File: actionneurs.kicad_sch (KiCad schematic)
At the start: 73 parts, among them J1 690367280876, J10 ESC_35_1_P, J11 690367280876, J12 ESC_35_2_S, J13 Alim Pompe, J14 690367280876, J6 ESC_35_1_P, J7 RGBA_LEDs, J9 ESC_35_1_S, Q1 G2302, Q10 G2302, Q11 G2302, Q12 G2302, Q13 G2302, Q14 G2302, Q15 G2302, Q16 G2302, Q17 G2302, Q2 G2302, Q3 G2302, Q4 G2302, Q5 G2302, Q9 G2302

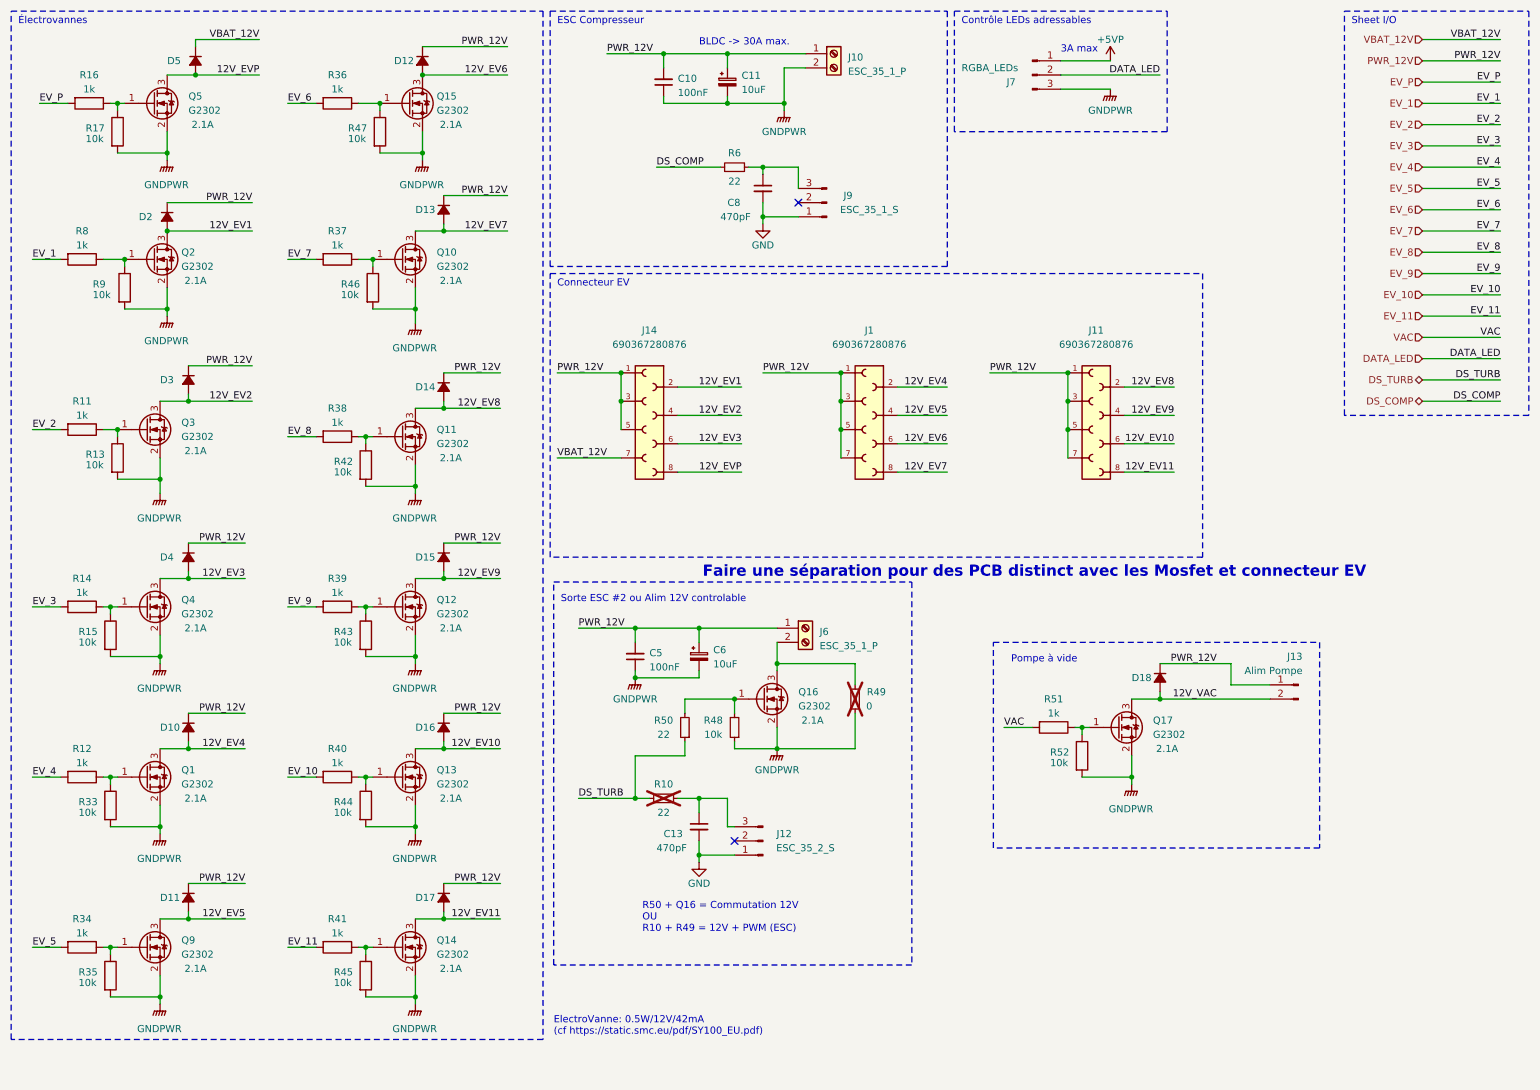
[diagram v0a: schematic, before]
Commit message: split des cartes
Todo: sync routage et ajout trou de fixation
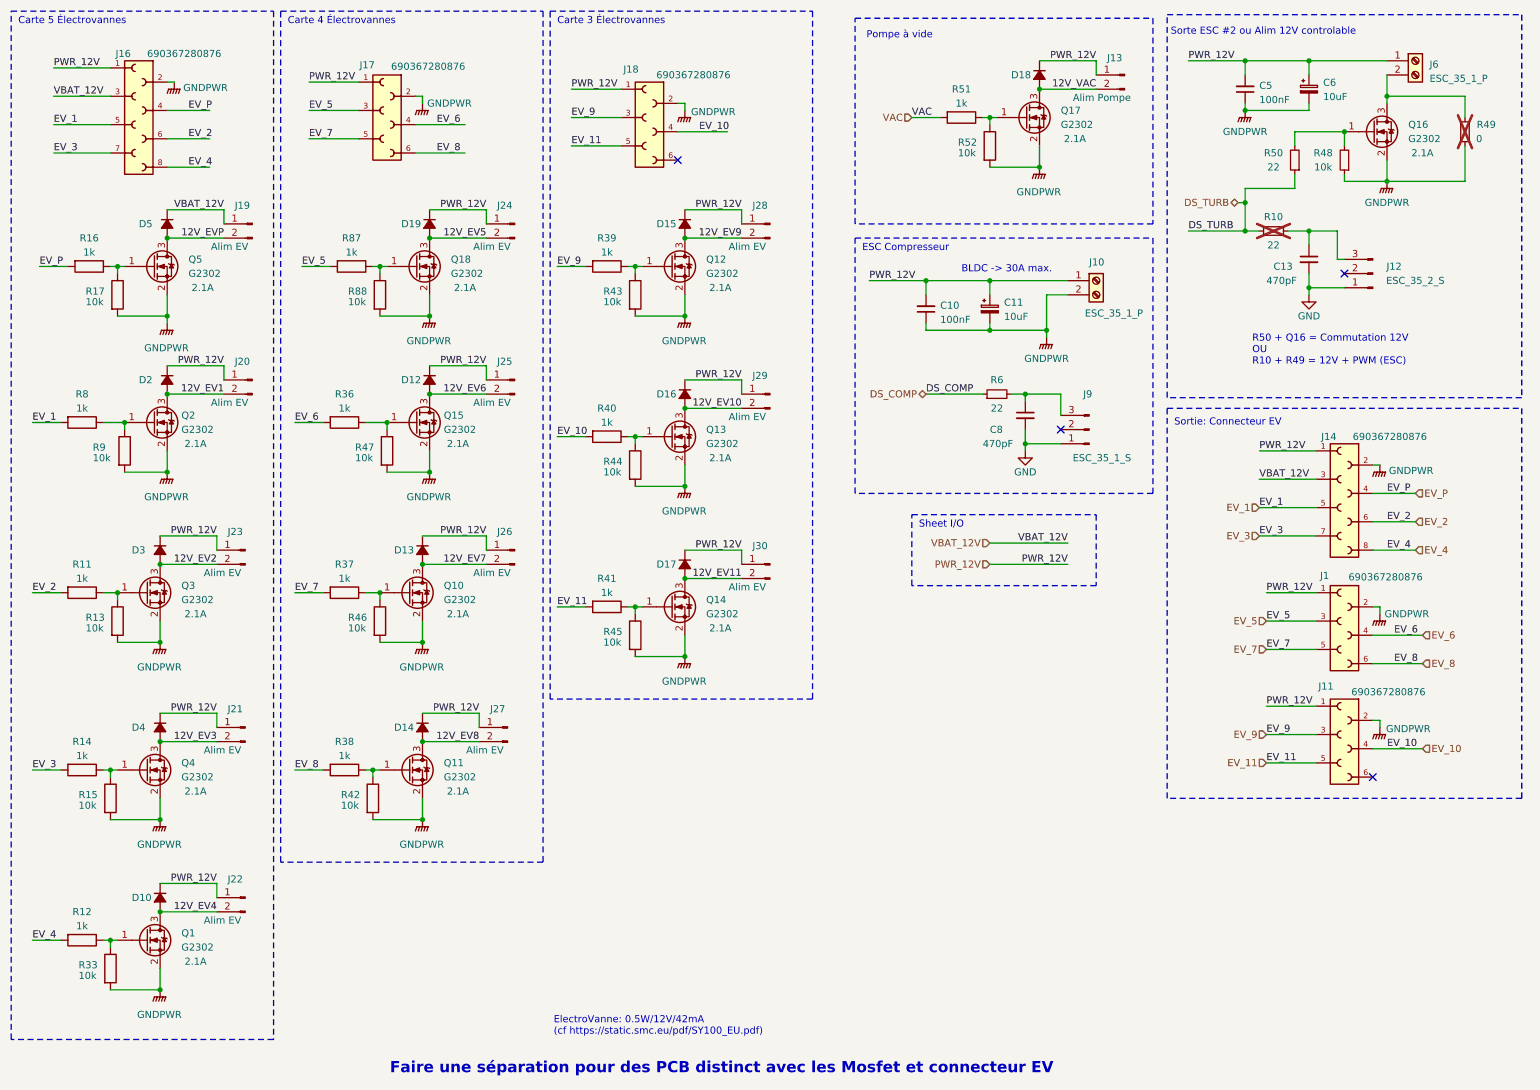
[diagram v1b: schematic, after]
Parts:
- removed D11: ~, Diode_SMD:D_SOD-123F, symbol Device:D_Small_Filled
- removed J7: RGBA_LEDs, Connector_PinHeader_2.54mm:PinHeader_1x03_P2.54mm_Vertical, symbol Connector:Conn_01x03_Pin
- removed Q9: G2302, Package_TO_SOT_SMD:SOT-23, symbol Device:Q_NMOS_GSD
- removed R34: 1k, Resistor_SMD:R_0603_1608Metric, symbol Device:R
- removed R35: 10k, Resistor_SMD:R_0603_1608Metric, symbol Device:R
- added D19: ~, Diode_SMD:D_SOD-123F, symbol Device:D_Small_Filled
- added J16: 690367280876, ConnectorsEvo:690367280876, symbol ConnectorsEvo:690367280876
- added J17, J18: 690367280876, ConnectorsEvo:690367280676, symbol ConnectorsEvo:690367280676
- added J19, J20, J21, J22, J23, J24, J25, J26, J27, J28, J29, J30: Alim EV, Connector_PinSocket_2.54mm:PinSocket_1x02_P2.54mm_Vertical, symbol Connector:Conn_01x02_Pin
- added Q18: G2302, Package_TO_SOT_SMD:SOT-23, symbol Device:Q_NMOS_GSD
- added R87: 1k, Resistor_SMD:R_0603_1608Metric, symbol Device:R
- added R88: 10k, Resistor_SMD:R_0603_1608Metric, symbol Device:R
- J1, J11: footprint ConnectorsEvo:690367280876 -> ConnectorsEvo:690367280676; symbol ConnectorsEvo:690367280876 -> ConnectorsEvo:690367280676; PART-NUMBER 690367280876 -> 690367280676; PINS 8 -> 6
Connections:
- net 12V_EV1: now also J20.2 (Pin_2); no longer J14.2
- net 12V_EV10: now also J29.2 (Pin_2); no longer J11.6
- net 12V_EV11: now also J30.2 (Pin_2); no longer J11.8
- net 12V_EV2: now also J23.2 (Pin_2); no longer J14.4
- net 12V_EV3: now also J21.2 (Pin_2); no longer J14.6
- net 12V_EV4: now also J22.2 (Pin_2); no longer J1.2
- net 12V_EV5: now also D19.2 (A), J24.2 (Pin_2), Q18.3 (D); no longer J1.4
- net 12V_EV6: now also J25.2 (Pin_2); no longer J1.6
- net 12V_EV7: now also J26.2 (Pin_2); no longer J1.8
- net 12V_EV8: now also J27.2 (Pin_2); no longer J11.2
- net 12V_EV9: now also J28.2 (Pin_2); no longer J11.4
- net 12V_EVP: now also J19.2 (Pin_2); no longer J14.8
- net EV_1: now also J14.5, J16.5
- net EV_10: now also J11.4, J18.4
- net EV_11: now also J11.5, J18.5
- net EV_2: now also J14.6, J16.6
- net EV_3: now also J14.7, J16.7
- net EV_4: now also J14.8, J16.8
- net EV_5: now also J1.3, J17.3, R87.2
- net EV_6: now also J1.4, J17.4
- net EV_7: now also J1.5, J17.5
- net EV_8: now also J1.6, J17.6
- net EV_9: now also J11.3, J18.3
- net EV_P: now also J14.4, J16.4
- net GNDPWR: now also J1.2, J11.2, J14.2, J16.2, J17.2, J18.2, Q18.2 (S), R88.2
- net PWR_12V: now also D19.1 (K), J16.1, J17.1, J18.1, J20.1 (Pin_1), J21.1 (Pin_1), J22.1 (Pin_1), J23.1 (Pin_1), J24.1 (Pin_1), J25.1 (Pin_1), J26.1 (Pin_1), J27.1 (Pin_1), J28.1 (Pin_1), J29.1 (Pin_1), J30.1 (Pin_1); no longer J1.3, J1.5, J1.7, J11.3, J11.5, J11.7, J14.3, J14.5
- net VBAT_12V: now also J14.3, J16.3, J19.1 (Pin_1); no longer J14.7
- new net: Q18.1 (G), R87.1, R88.1
- no-connect marks 2 -> 4
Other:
- note added: "Carte 3 Électrovannes"
- note added: "Carte 4 Électrovannes"
- note added: "Carte 5 Électrovannes"
- note added: "Sortie: Connecteur EV"
- note removed: "3A max"
- note removed: "Connecteur EV"
- note removed: "Contrôle LEDs adressables"
- note removed: "Électrovannes"
- moved on the sheet: C10, C11, C13, C5, C6, C8, D10, D12, D13, D14, D18, D2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

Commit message: optimisation empreinte passif (TODO fp diode), TODO ajouter LED temoin diverse, groupement sur PCB des nouveaux composant
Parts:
- R49: footprint Resistor_SMD:R_0603_1608Metric -> Jumper:SolderJumper-2_P1.3mm_Open_RoundedPad1.0x1.5mm; symbol Device:R_Small -> Jumper:SolderJumper_2_Open
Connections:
- net EV_1: now also J14.3, J16.3; no longer J14.5, J16.5
- net EV_2: now also J14.4, J16.4; no longer J14.6, J16.6
- net EV_3: now also J14.5, J16.5; no longer J14.7, J16.7
- net EV_4: now also J14.6, J16.6; no longer J14.8, J16.8
- net EV_P: now also J14.8, J16.8; no longer J14.4, J16.4
- net GNDPWR: now also R49.2 (B); no longer R49.1
- net VBAT_12V: now also J14.7, J16.7; no longer J14.3, J16.3
- net at J6.2 (Pin_2), Q16.3 (D): now also R49.1 (A); no longer R49.2
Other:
- note removed: "Faire une séparation pour des PCB distinct avec les Mosfet et connecteur EV"
- moved on the sheet: C5, C6, Q16, R48, R50

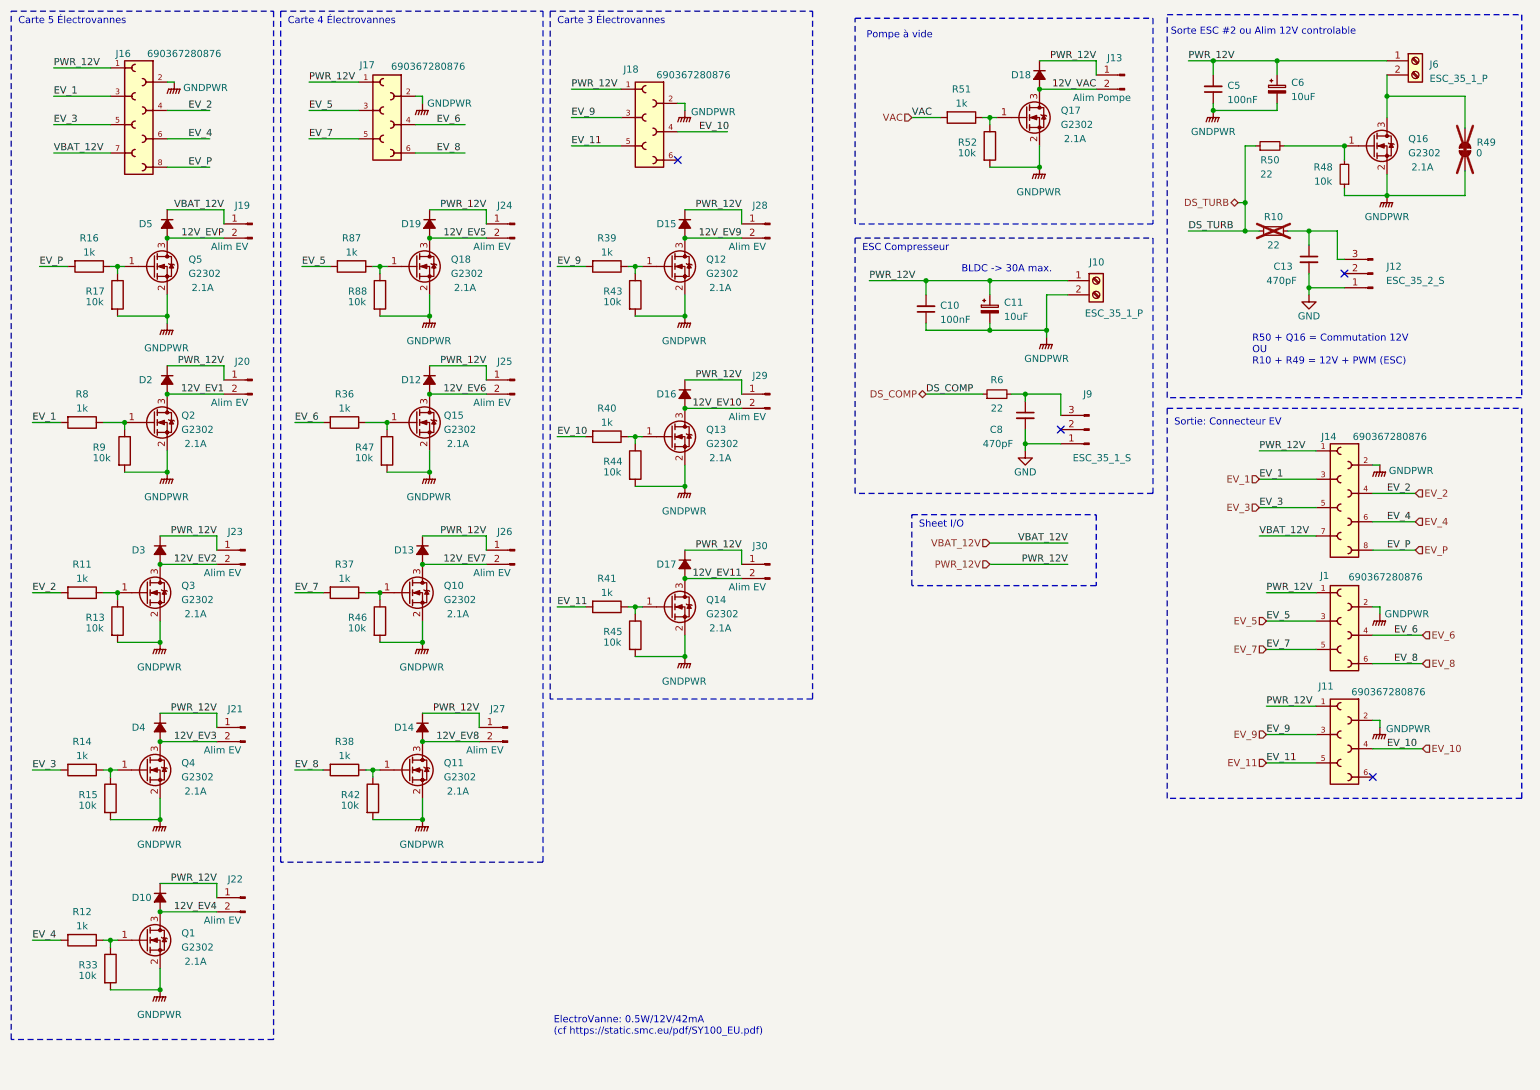
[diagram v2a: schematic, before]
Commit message: placement en cours, remplacement diode schotcky, customisation empreinte capteur pression, suppression R pour les signaux figé du uC (SW, BOOT, etc). TODO avancer placement, ajouter LED
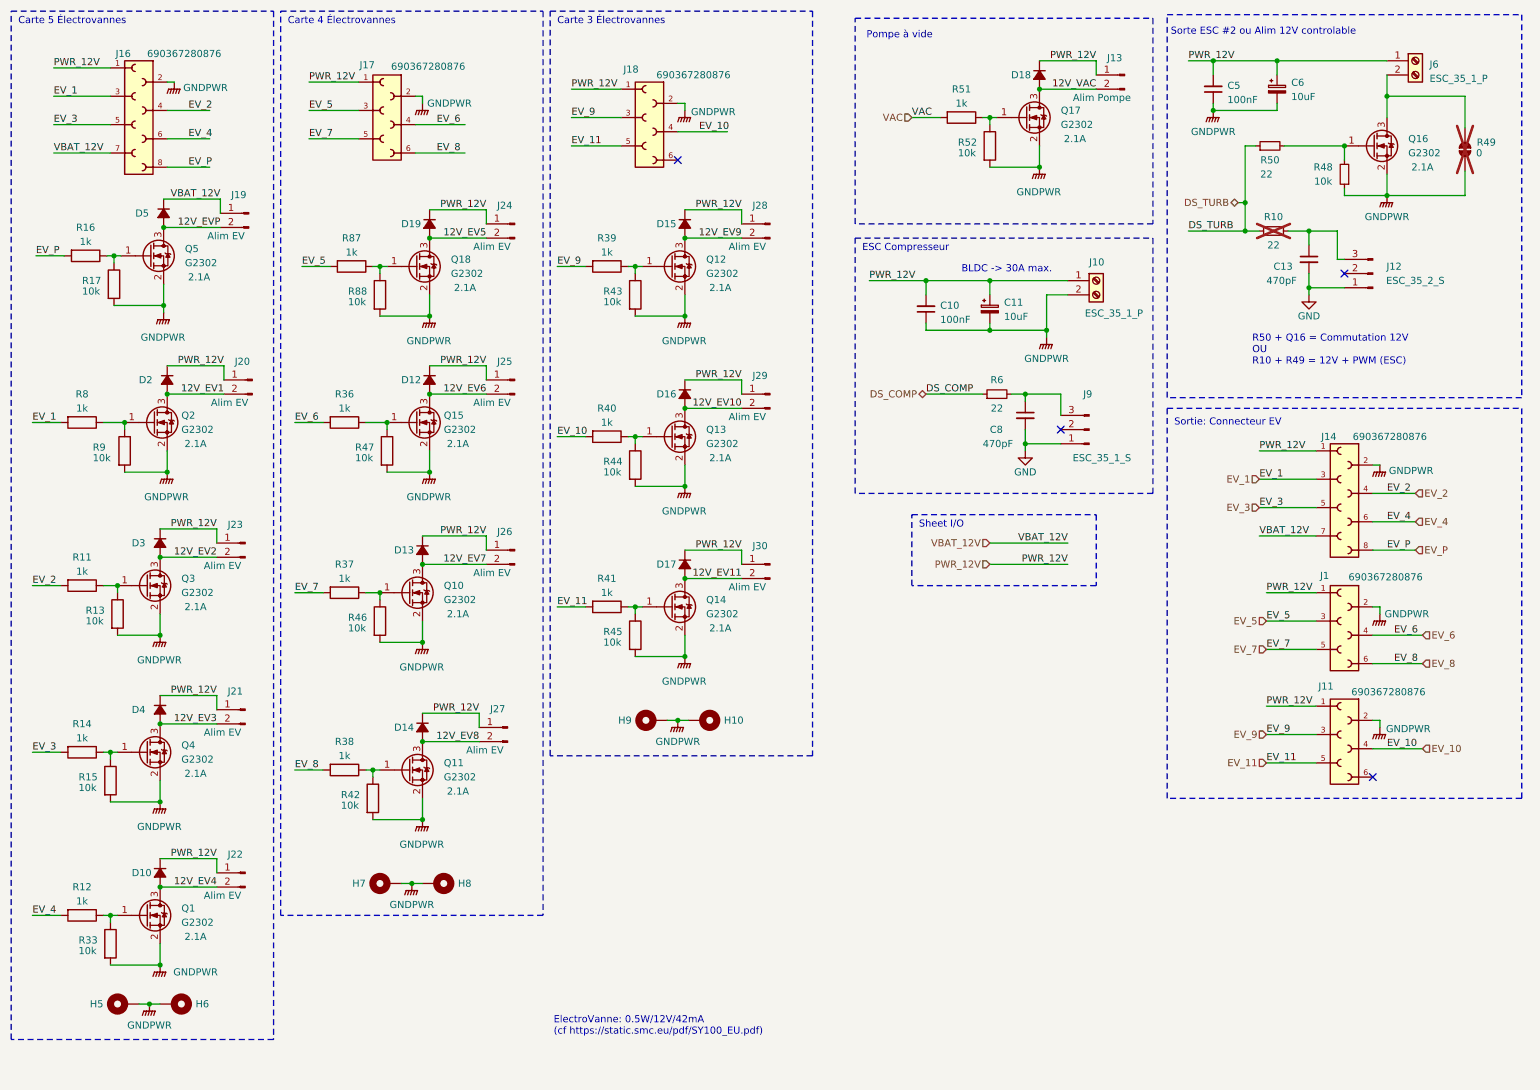
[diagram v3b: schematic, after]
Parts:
- added H10, H5, H6, H7, H8, H9: MountingHole_Pad, MountingHole:MountingHole_3.2mm_M3_Pad, symbol Mechanical:MountingHole_Pad
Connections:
- net GNDPWR: now also H10.1, H5.1, H6.1, H7.1, H8.1, H9.1
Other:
- moved on the sheet: D10, D3, D4, D5, J19, J21, J22, J23, Q1, Q3, Q4, Q5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

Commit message: placement composant (carte distributeur)
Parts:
- J19, J20, J21, J22, J23, J24, J25, J26, J27, J28, J29, J30: footprint Connector_PinSocket_2.54mm:PinSocket_1x02_P2.54mm_Vertical -> 12V-actuators_pcb:PinSocket_1x02_P2.54mm_Vertical_widePad
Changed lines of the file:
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@@
 			)
 		)
-		(property "Footprint" "Connector_PinSocket_2.54mm:PinSocket_1x02_P2.54mm_Vertical"
+		(property "Footprint" "12V-actuators_pcb:PinSocket_1x02_P2.54mm_Vertical_widePad"
 			(at 148.59 81.28 0)
 			(effects
@@
 			)
 		)
-		(property "Footprint" "Connector_PinSocket_2.54mm:PinSocket_1x02_P2.54mm_Vertical"
+		(property "Footprint" "12V-actuators_pcb:PinSocket_1x02_P2.54mm_Vertical_widePad"
 			(at 102.87 109.22 0)
 			(effects
@@
 			)
 		)
-		(property "Footprint" "Connector_PinSocket_2.54mm:PinSocket_1x02_P2.54mm_Vertical"
+		(property "Footprint" "12V-actuators_pcb:PinSocket_1x02_P2.54mm_Vertical_widePad"
 			(at 102.87 78.74 0)
 			(effects
@@
 			)
 		)
-		(property "Footprint" "Connector_PinSocket_2.54mm:PinSocket_1x02_P2.54mm_Vertical"
+		(property "Footprint" "12V-actuators_pcb:PinSocket_1x02_P2.54mm_Vertical_widePad"
 			(at 101.6 140.97 0)
 			(effects
@@
 			)
 		)
-		(property "Footprint" "Connector_PinSocket_2.54mm:PinSocket_1x02_P2.54mm_Vertical"
+		(property "Footprint" "12V-actuators_pcb:PinSocket_1x02_P2.54mm_Vertical_widePad"
 			(at 102.87 50.8 0)
 			(effects
@@
 			)
 		)
-		(property "Footprint" "Connector_PinSocket_2.54mm:PinSocket_1x02_P2.54mm_Vertical"
+		(property "Footprint" "12V-actuators_pcb:PinSocket_1x02_P2.54mm_Vertical_widePad"
 			(at 55.245 48.895 0)
 			(effects
@@
 			)
 		)
-		(property "Footprint" "Connector_PinSocket_2.54mm:PinSocket_1x02_P2.54mm_Vertical"
+		(property "Footprint" "12V-actuators_pcb:PinSocket_1x02_P2.54mm_Vertical_widePad"
 			(at 55.88 78.74 0)
 			(effects
@@
 			)
 		)
-		(property "Footprint" "Connector_PinSocket_2.54mm:PinSocket_1x02_P2.54mm_Vertical"
+		(property "Footprint" "12V-actuators_pcb:PinSocket_1x02_P2.54mm_Vertical_widePad"
 			(at 148.59 50.8 0)
 			(effects
@@
 			)
 		)
-		(property "Footprint" "Connector_PinSocket_2.54mm:PinSocket_1x02_P2.54mm_Vertical"
+		(property "Footprint" "12V-actuators_pcb:PinSocket_1x02_P2.54mm_Vertical_widePad"
 			(at 54.61 137.795 0)
 			(effects
@@
 			)
 		)
-		(property "Footprint" "Connector_PinSocket_2.54mm:PinSocket_1x02_P2.54mm_Vertical"
+		(property "Footprint" "12V-actuators_pcb:PinSocket_1x02_P2.54mm_Vertical_widePad"
 			(at 54.61 167.005 0)
 			(effects
@@
 			)
 		)
-		(property "Footprint" "Connector_PinSocket_2.54mm:PinSocket_1x02_P2.54mm_Vertical"
+		(property "Footprint" "12V-actuators_pcb:PinSocket_1x02_P2.54mm_Vertical_widePad"
 			(at 54.61 107.95 0)
 			(effects
@@
 			)
 		)
-		(property "Footprint" "Connector_PinSocket_2.54mm:PinSocket_1x02_P2.54mm_Vertical"
+		(property "Footprint" "12V-actuators_pcb:PinSocket_1x02_P2.54mm_Vertical_widePad"
 			(at 148.59 111.76 0)
 			(effects
